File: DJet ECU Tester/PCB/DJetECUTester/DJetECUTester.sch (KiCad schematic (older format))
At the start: 41 parts, among them J1 ISP, J10 ECU3, J2 ECU1, J4 12V 4A IN (5.5/2.5), J5 12V IN, J6 MPS, J7 Conn_01x01, J8 Conn_01x01, J9 ECU2, U1 ATmega328P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

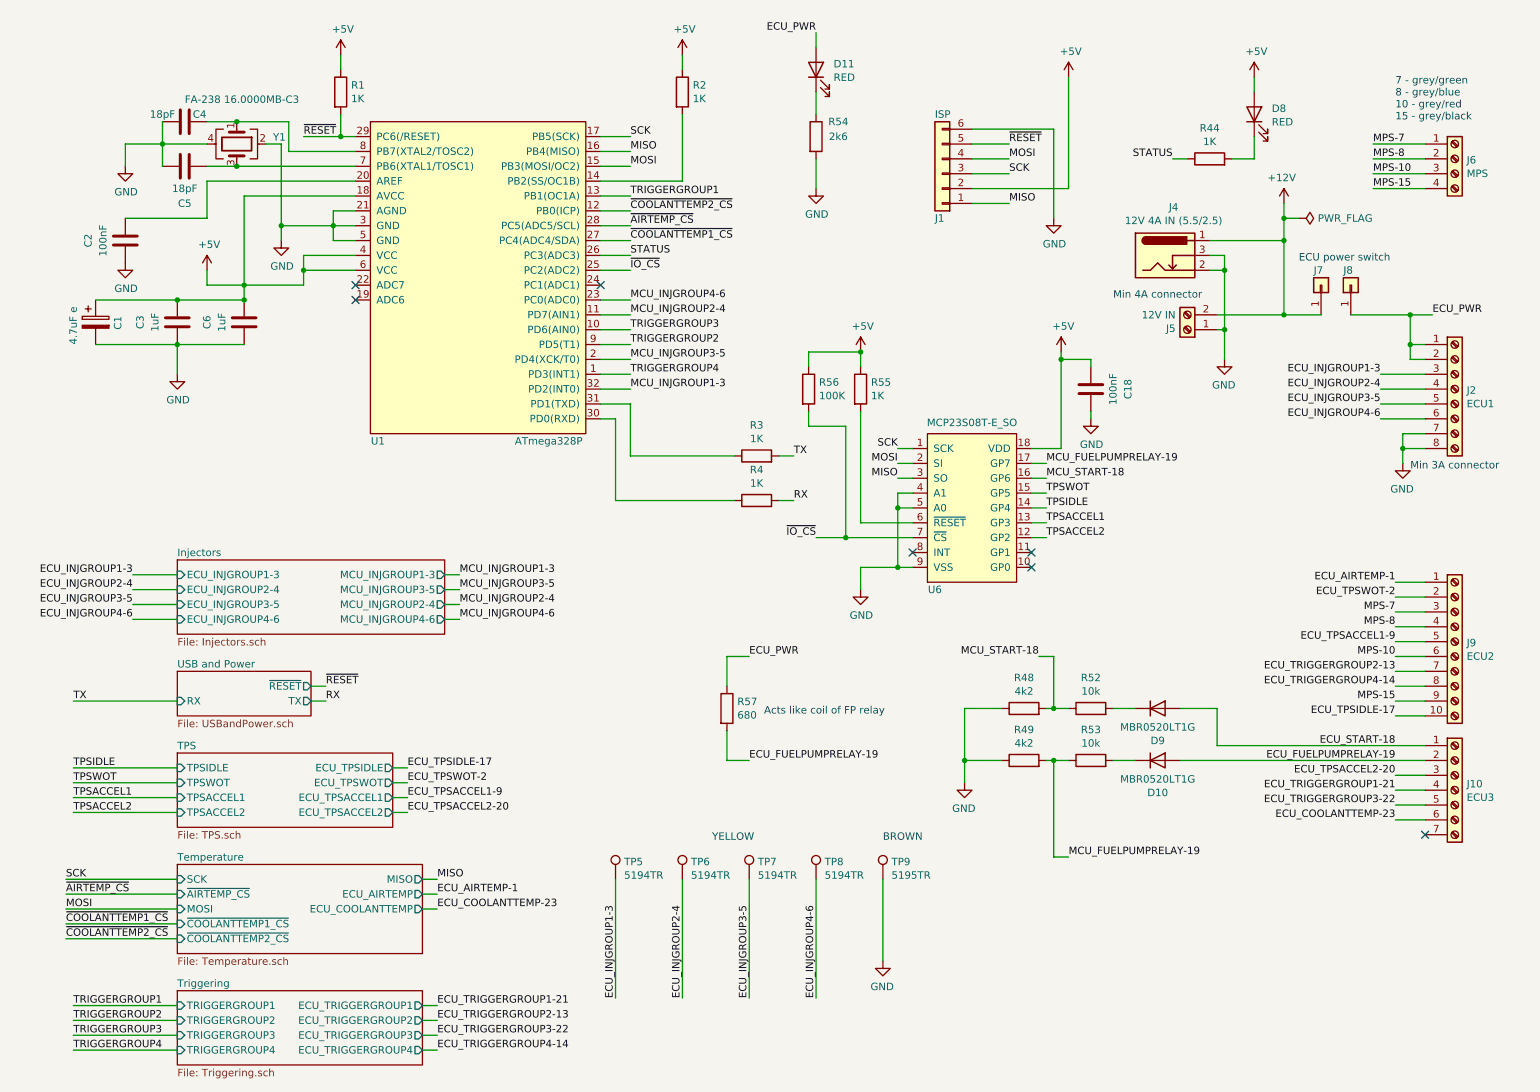
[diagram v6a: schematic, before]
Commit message: Changed start signal from ECU output to ECU input.
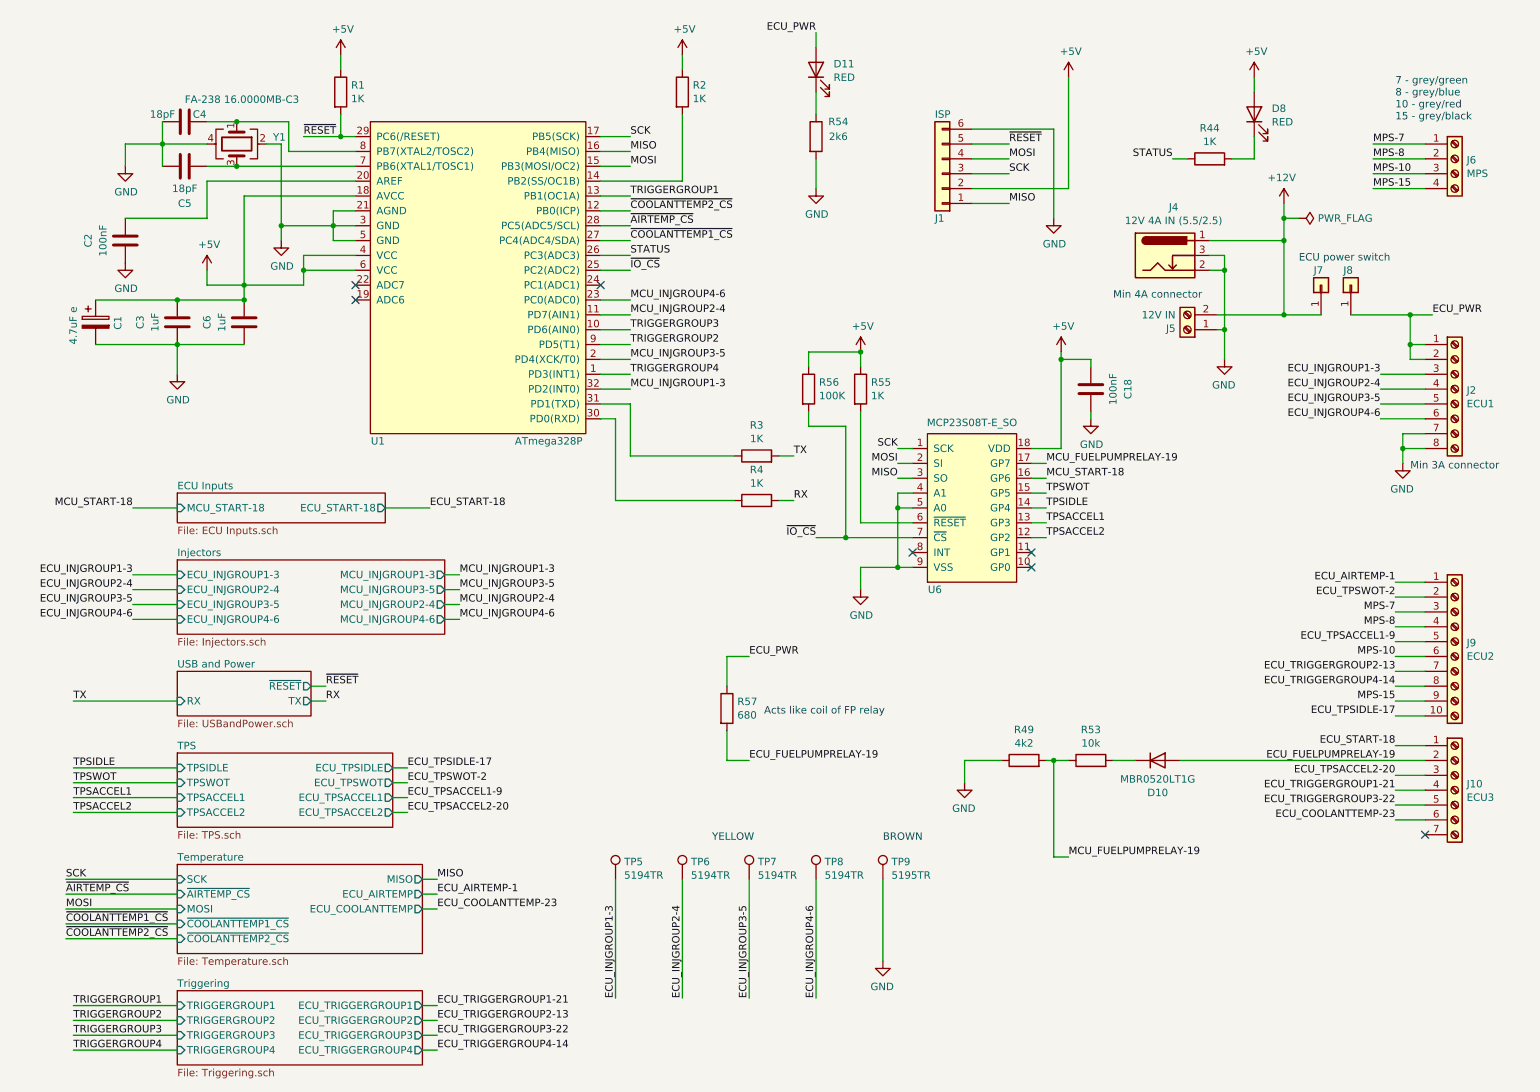
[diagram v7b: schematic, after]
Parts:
- removed D9: MBR0520LT1G, Britishideas:SOD-123, symbol Device:D
- removed R48: 4k2, Resistor_SMD:R_0805_2012Metric, symbol Device:R
- removed R52: 10k, Resistor_SMD:R_0805_2012Metric, symbol Device:R
- R57: manf# (none) -> CRCW1206680RFKEAHP
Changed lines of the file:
@@
 $Descr A4 11693 8268
 encoding utf-8
-Sheet 1 6
+Sheet 1 7
 Title "D-Jetronic ECU Tester"
-Date "2022-10-14"
+Date "2022-10-15"
 Rev "2.1"
 Comp "(C) Britishideas 2021-2022"
@@
 ~IO_CS
 NoConn ~ 4550 2400
-NoConn ~ 7450 4200
 NoConn ~ 7450 4300
 Text Label 4750 1900 0    50   ~ 0
@@
 Wire Wire Line
 	7000 5600 7000 5750
-$Comp
-L Device:R R52
-U 1 1 632EA45C
-P 7850 5250
-F 0 "R52" V 8057 5250 50  0000 C CNN
-F 1 "10k" V 7966 5250 50  0000 C CNN
-F 2 "Resistor_SMD:R_0805_2012Metric" V 7780 5250 50  0001 C CNN
-F 3 "~" H 7850 5250 50  0001 C CNN
-	1    7850 5250
-	0    -1   -1   0
-$EndComp
-$Comp
-L Device:R R48
-U 1 1 632EA6C2
-P 7400 5250
-F 0 "R48" V 7607 5250 50  0000 C CNN
-F 1 "4k2" V 7516 5250 50  0000 C CNN
-F 2 "Resistor_SMD:R_0805_2012Metric" V 7330 5250 50  0001 C CNN
-F 3 "~" H 7400 5250 50  0001 C CNN
-	1    7400 5250
-	0    -1   -1   0
-$EndComp
-Wire Wire Line
-	8150 5250 8000 5250
-Wire Wire Line
-	7700 5250 7600 5250
-Wire Wire Line
-	7250 5250 7000 5250
-Wire Wire Line
-	7000 5250 7000 5600
-Connection ~ 7000 5600
 Text Label 7700 6250 0    50   ~ 0
 MCU_FUELPUMPRELAY-19
@@
 Wire Wire Line
 	7600 5600 7550 5600
-Text Label 7500 4900 2    50   ~ 0
-MCU_START-18
-Wire Wire Line
-	7500 4900 7600 4900
-Wire Wire Line
-	7600 4900 7600 5250
-Connection ~ 7600 5250
-Wire Wire Line
-	7600 5250 7550 5250
 Text Label 7550 3700 0    50   ~ 0
 MCU_START-18
@@
 	1    0    0    -1
 $EndComp
-$Comp
-L Device:D D?
-U 1 1 633559ED
-P 8300 5250
-AR Path="/63357965/633559ED" Ref="D?"  Part="1"
-AR Path="/633559ED" Ref="D9"  Part="1"
-F 0 "D9" H 8300 5033 50  0000 C CNN
-F 1 "MBR0520LT1G" H 8300 5124 50  0000 C CNN
-F 2 "Britishideas:SOD-123" H 8300 5250 50  0001 C CNN
-F 3 "~" H 8300 5250 50  0001 C CNN
-	1    8300 5250
-	1    0    0    -1
-$EndComp
 Wire Wire Line
 	8000 5600 8150 5600
 Wire Wire Line
 	8450 5600 10100 5600
-Wire Wire Line
-	8700 5500 8700 5250
-Wire Wire Line
-	8700 5250 8450 5250
-Wire Wire Line
-	8700 5500 10100 5500
 $Comp
 L Connector:Barrel_Jack_Switch J4
@@
 F 2 "Resistor_SMD:R_1206_3216Metric" V 5330 5250 50  0001 C CNN
 F 3 "~" H 5400 5250 50  0001 C CNN
+F 4 "CRCW1206680RFKEAHP" H 5400 5250 50  0001 C CNN "manf#"
 	1    5400 5250
 	1    0    0    -1
@@
 Text Notes 5650 5300 0    50   ~ 0
 Acts like coil of FP relay
+Wire Wire Line
+	10100 5500 9900 5500
+NoConn ~ 7450 4200
+$Sheet
+S 1700 3800 1400 200
+U 634E02FB
+F0 "ECU Inputs" 50
+F1 "ECU Inputs.sch" 50
+F2 "MCU_START-18" I L 1700 3900 50
+F3 "ECU_START-18" O R 3100 3900 50
+$EndSheet
+Text Label 1400 3900 2    50   ~ 0
+MCU_START-18
+Text Label 3400 3900 0    50   ~ 0
+ECU_START-18
+Wire Wire Line
+	1400 3900 1700 3900
+Wire Wire Line
+	3400 3900 3100 3900
 $EndSCHEMATC

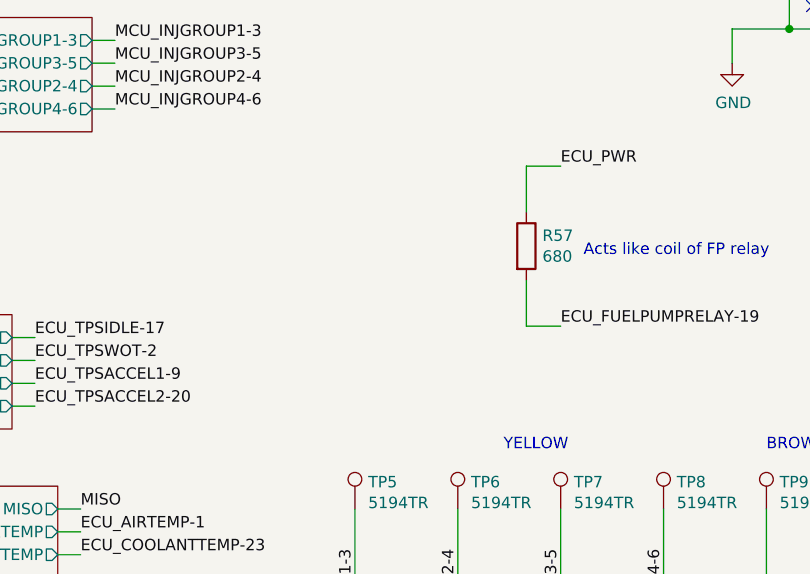
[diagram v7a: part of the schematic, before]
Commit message: Added connector for cooling fan.
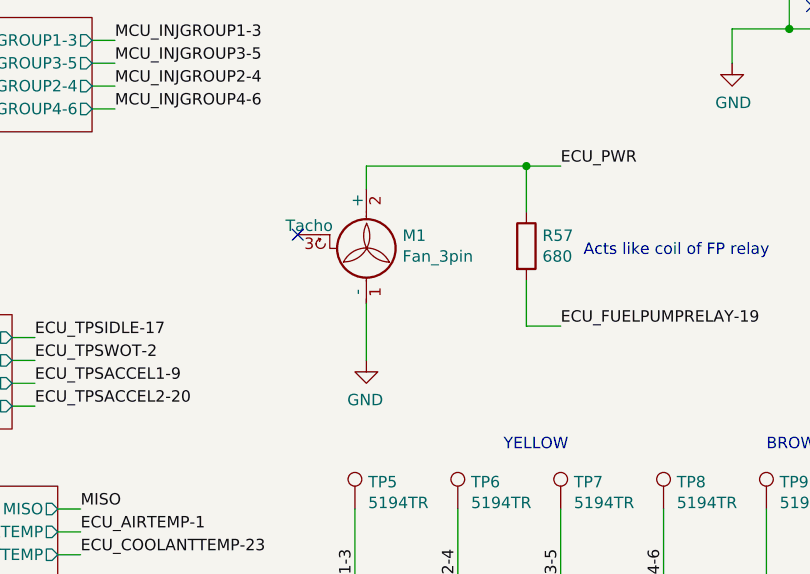
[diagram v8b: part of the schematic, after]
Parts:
- added M1: Fan_3pin, Connector:FanPinHeader_1x03_P2.54mm_Vertical, symbol BritishIdeas:Fan_3pin
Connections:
- net ECU_PWR: now also M1.2 (+)
- net GND: now also M1.1 (-)
- no-connect marks 7 -> 8
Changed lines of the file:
@@
 Wire Wire Line
 	3400 3900 3100 3900
+Wire Wire Line
+	5400 4900 4700 4900
+Wire Wire Line
+	4700 4900 4700 5000
+Connection ~ 5400 4900
+$Comp
+L power:GND #PWR077
+U 1 1 634D17F4
+P 4700 5750
+AR Path="/634D17F4" Ref="#PWR077"  Part="1"
+AR Path="/60479334/634D17F4" Ref="#PWR?"  Part="1"
+F 0 "#PWR077" H 4700 5500 50  0001 C CNN
+F 1 "GND" H 4705 5577 50  0000 C CNN
+F 2 "" H 4700 5750 50  0001 C CNN
+F 3 "" H 4700 5750 50  0001 C CNN
+	1    4700 5750
+	-1   0    0    -1
+$EndComp
+Wire Wire Line
+	4700 5750 4700 5500
+NoConn ~ 4400 5200
+$Comp
+L BritishIdeas:Fan_3pin M1
+U 1 1 63504226
+P 4700 5200
+F 0 "M1" H 4858 5196 50  0000 L CNN
+F 1 "Fan_3pin" H 4858 5105 50  0000 L CNN
+F 2 "Connector:FanPinHeader_1x03_P2.54mm_Vertical" H 4700 5110 50  0001 C CNN
+F 3 "http://www.hardwarecanucks.com/forum/attachments/new-builds/16287d1330775095-help-chassis-power-fan-connectors-motherboard-asus_p8z68.jpg" H 4700 5110 50  0001 C CNN
+	1    4700 5200
+	1    0    0    -1
+$EndComp
 $EndSCHEMATC
